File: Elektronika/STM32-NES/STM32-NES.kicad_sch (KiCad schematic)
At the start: 8 parts, among them J1 LCD Display 2.8 Cala, J2 Power Supply 5V 3A, J3 PAD, U1 NUCLEO-F446RE

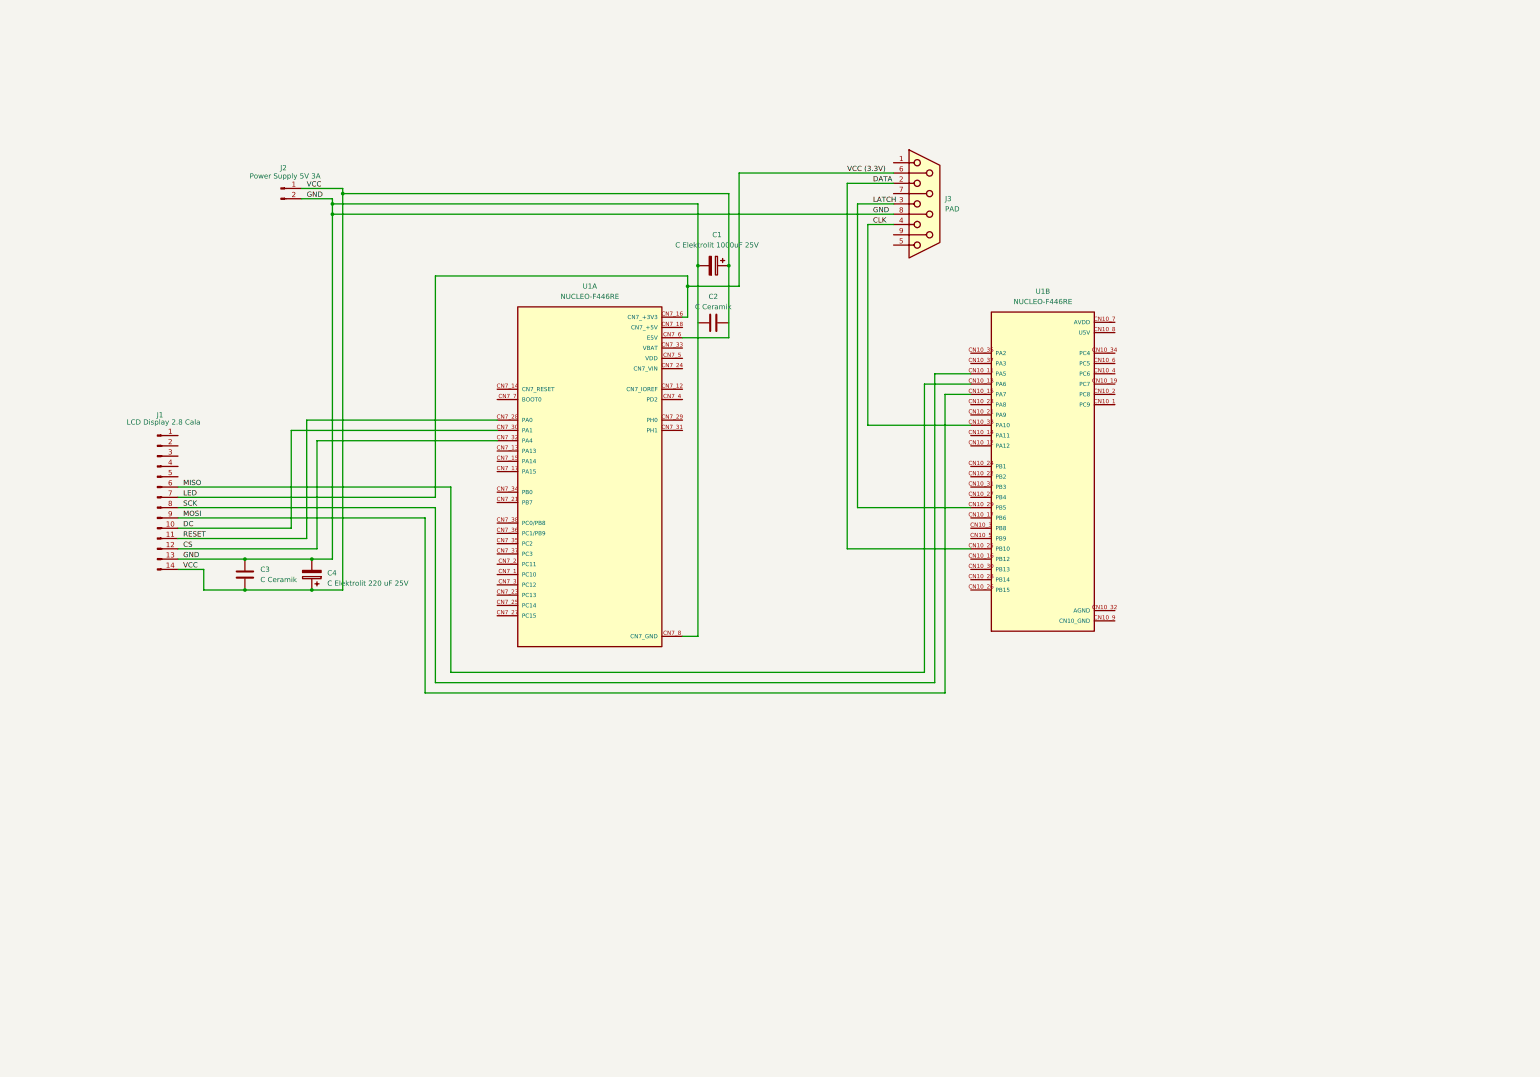
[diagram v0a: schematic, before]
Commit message: I2S przeniesiono z I2S2 na I2S3 eliminując szumy z SPI1. Bufor sampli muzyki w SRAM2, dzięki czemu DMA do LCD i DMA po I2S może chodzić równolegle.
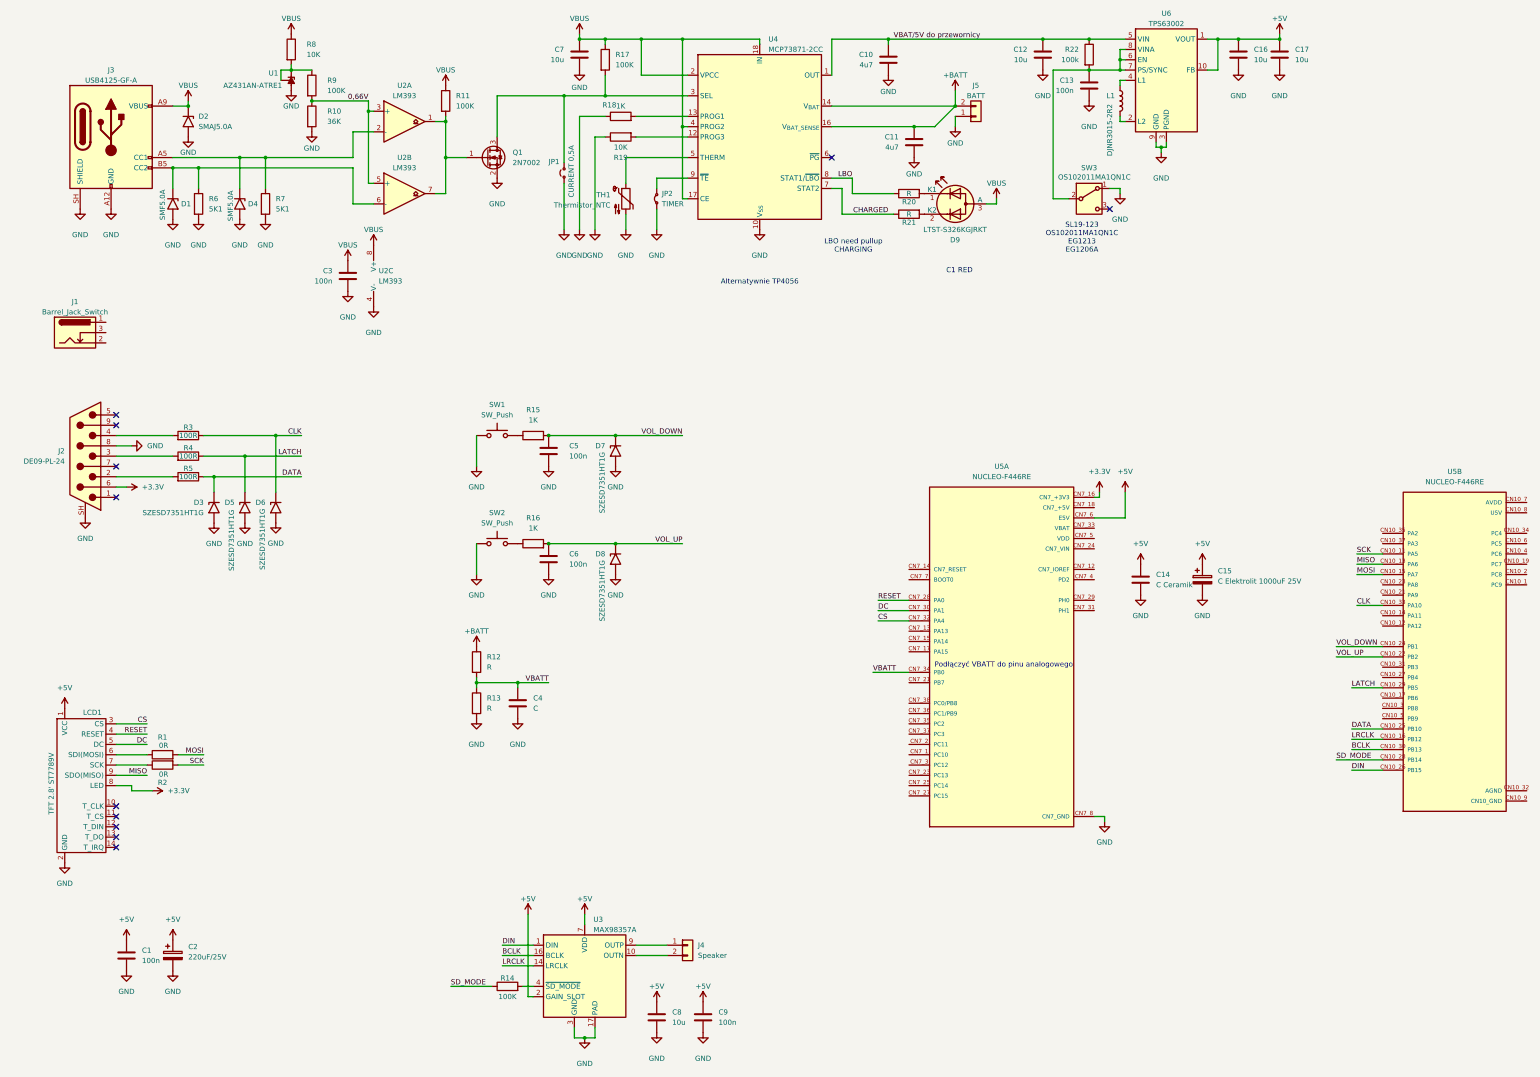
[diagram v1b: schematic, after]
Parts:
- removed C1: C Elektrolit 1000uF 25V, symbol Device:C_Polarized
- removed C4: C Elektrolit 220 uF 25V, symbol Device:C_Polarized
- removed J1: LCD Display 2.8 Cala, symbol Connector:Conn_01x14_Pin
- removed J2: Power Supply 5V 3A, symbol Connector:Conn_01x02_Pin
- removed J3: PAD, symbol Connector:DE9_Socket
- added C1, C13, C5, C6: 100n, symbol Device:C
- added C10: 4u7, Capacitor_SMD:C_0805_2012Metric, symbol Device:C
- added C11: 4u7, symbol Device:C
- added C12: 10u, symbol Device:C
- added C15: C Elektrolit 1000uF 25V, symbol Device:C_Polarized
- added C16, C17, C7, C8: 10u, Capacitor_SMD:C_0805_2012Metric, symbol Device:C
- added C2: 220uF/25V, symbol Device:C_Polarized
- added C4: C, symbol Device:C
- added C9: 100n, Capacitor_SMD:C_0805_2012Metric, symbol Device:C
- added D1, D4: SMF5.0A, Diode_SMD:D_SOD-123F, symbol Diode:SMF5V0A
- added D2: SMAJ5.0A, Diode_SMD:D_SMA, symbol Diode:SMAJ5.0A
- added D3, D5, D6, D7, D8: SZESD7351HT1G, Diode_SMD:D_SOD-323_HandSoldering, symbol Diode:SMF5V0A
- added D9: LTST-S326KGJRKT, LED_SMD:LED_LiteOn_LTST-S326, symbol Device:LED_Dual_KKA
- added J1: Barrel_Jack_Switch, symbol Connector:Barrel_Jack_Switch
- added J2: DE09-PL-24, Connector_Dsub:DSUB-9_Pins_Horizontal_P2.77x2.84mm_EdgePinOffset4.94mm_Housed_MountingHolesOffset4.94mm, symbol Connector:DE9_Pins_MountingHoles
- added J3: USB4125-GF-A, Connector_USB:USB_C_Receptacle_HRO_TYPE-C-31-M-17, symbol Connector:USB_C_Receptacle_PowerOnly_6P
- added J4: Speaker, Connector_JST:JST_PH_B2B-PH-K_1x02_P2.00mm_Vertical, symbol Connector_Generic:Conn_01x02
- added J5: BATT, Connector_JST:JST_PH_B2B-PH-K_1x02_P2.00mm_Vertical, symbol Connector_Generic:Conn_01x02
- added JP1: CURRENT 0,5A, symbol Jumper:Jumper_2_Small_Open
- added JP2: TIMER, symbol Jumper:Jumper_2_Small_Bridged
- added L1: DJNR3015-2R2, Inductor_SMD:L_Coilcraft_LPS3010, symbol Device:L
- added LCD1: TFT 2.8' ST7789V, STM32-NES:TFT 2.8' ST7789V, symbol STM32-NES:TFT_240x320_2.8{dblquote}_SPI_ST7789V
- added Q1: 2N7002, Package_TO_SOT_SMD:SOT-23, symbol Transistor_FET:2N7002
- added R1, R2: 0R, symbol Device:R
- added R10: 36K, symbol Device:R
- added R11, R14, R17, R9: 100K, symbol Device:R
- added R12, R13, R20, R21: R, symbol Device:R
- added R15, R16, R18: 1K, symbol Device:R
- added R19, R8: 10K, symbol Device:R
- added R22: 100k, symbol Device:R
- added R3, R4, R5: 100R, symbol Device:R
- added R6, R7: 5K1, symbol Device:R
- added SW1, SW2: SW_Push, symbol Switch:SW_Push
- added SW3: OS102011MA1QN1C, Button_Switch_THT:SW_Slide_SPDT_Angled_CK_OS102011MA1Q, symbol Switch:SW_SPDT
- added TH1: Thermistor_NTC, symbol Device:Thermistor_NTC
- added U1: AZ431AN-ATRE1, Package_TO_SOT_SMD:SOT-23, symbol Reference_Voltage:TL432DBZ
- added U2: LM393, symbol Comparator:LM393
- added U3: MAX98357A, Package_DFN_QFN:TQFN-16-1EP_3x3mm_P0.5mm_EP1.23x1.23mm, symbol Audio:MAX98357A
- added U4: MCP73871-2CC, Package_DFN_QFN:QFN-20-1EP_4x4mm_P0.5mm_EP2.5x2.5mm, symbol Battery_Management:MCP73871-2CC
- added U6: TPS63002, Package_SON:Texas_DRC0010J_ThermalVias, symbol Regulator_Switching:TPS63002
- C3: value C Ceramik -> 100n
- U5: renamed from U1; footprint NUCLEO-F446RE:MODULE_NUCLEO-F446RE -> NUCLEO F446:MODULE_NUCLEO-F446RE
- renumbered C2 to C14
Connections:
- net CLK: now also D6.1 (A1), R3.1
- net CN7_GND: now also C14.1, C1.1, C10.2, C11.2, C12.2, C13.2, C15.2, C16.2, C17.2, C2.2, C4.2, C5.2, C6.2, C7.2, C8.2, C9.2, D1.2 (A2), D2.2 (A2), D3.2 (A2), D4.2 (A2), D5.2 (A2), D7.2 (A2), D8.2 (A2), J2.8, J2.SH (PAD), J3.A12 (GND), J3.B12 (GND), J3.SH (SHIELD), J5.1 (Pin_1), JP1.1 (A), JP2.1 (A), LCD1.2 (GND), Q1.2 (S), R10.2, R13.2, R18.1, R19.1, R6.2, R7.2, SW1.1, SW2.1, SW3.1 (A), TH1.2, U1.3 (A), U2.4 (V-), U3.11 (GND), U3.15 (GND), U3.17 (PAD), U3.3 (GND), U4.10 (V_{SS}), U4.11 (V_{SS}), U4.21 (V_{SS}), U6.11 (PGND), U6.3 (PGND), U6.9 (GND)
- net CS: now also LCD1.3 (CS)
- net DATA: now also D3.1 (A1), R5.1
- net DC: now also LCD1.5 (DC)
- net LATCH: now also D5.1 (A1), R4.1
- net MISO: now also LCD1.9 (SDO(MISO))
- net MOSI: now also R1.2
- net RESET: now also LCD1.4 (RESET)
- net SCK: now also R2.2
- net LRCLK: now reaches U5.CN10_16 (PB12)
- net LRCLK: now also U3.14 (LRCLK)
- net VOL_UP: now reaches U5.CN10_22 (PB2)
- net VOL_UP: now also C6.1, D8.1 (A1), R16.2
- net VOL_DOWN: now reaches U5.CN10_24 (PB1)
- net VOL_DOWN: now also C5.1, D7.1 (A1), R15.2
- net DIN: now reaches U5.CN10_26 (PB15)
- net DIN: now also U3.1 (DIN)
- net SD_MODE: now reaches U5.CN10_28 (PB14)
- net SD_MODE: now also R14.1
- net BCLK: now reaches U5.CN10_30 (PB13)
- net BCLK: now also U3.16 (BCLK)
- net VBATT: now reaches U5.CN7_34 (PB0)
- net VBATT: now also C4.1, R12.2, R13.1
- net +5V: now reaches C14.2
- net +5V: now also U5.CN7_6 (E5V), C1.2, C15.1, C16.1, C17.1, C2.1, C8.1, C9.1, LCD1.1 (VCC), U3.2 (GAIN_SLOT), U3.7 (VDD), U3.8 (VDD), U6.1 (VOUT), U6.10 (FB)
- net LED renamed +3.3V
- net +3.3V: now also J2.6, LCD1.8 (LED)
- net VCC renamed VBUS
- net VBUS: now also C7.1, D2.1 (A1), D9.3 (A), J3.A9 (VBUS), J3.B9 (VBUS), R11.1, R17.1, R8.1, U2.8 (V+), U4.17 (CE), U4.18 (IN), U4.19 (IN), U4.2 (VPCC), U4.4 (PROG2); no longer U5.CN7_6 (E5V)
- new net: J2.4, R3.2
- new net: LCD1.6 (SDI(MOSI)), R1.1
- new net: R15.1, SW1.2
- new net: R19.2, U4.12 (PROG3)
- new net: R18.2, U4.13 (PROG1)
- new net: JP1.2 (B), Q1.3 (D), R17.2, U4.3 (SEL)
- new net: TH1.1, U4.5 (THERM)
- new net: JP2.2 (B), U4.9 (~{TE})
- new net: J2.2, R5.2
- new net: C13.1, R22.2, SW3.2 (B), U6.6 (EN), U6.7 (PS/SYNC), U6.8 (VINA)
- new net: J2.3, R4.2
- new net: Q1.1 (G), R11.2, U2.1, U2.7
- new net: D4.1 (A1), J3.A5 (CC1), R7.1, U2.2 (-)
- new net: J4.2 (Pin_2), U3.10 (OUTN)
- new net: R14.2, U3.4 (~{SD_MODE})
- new net: J4.1 (Pin_1), U3.9 (OUTP)
- new net: D1.1 (A1), J3.B5 (CC2), R6.1, U2.6 (-)
- new net: D9.1 (K1), R20.2
- new net: D9.2 (K2), R21.2
- new net: R8.2, R9.1, U1.1 (REF), U1.2 (K)
- new net: L1.1, U6.4 (L1)
- new net: L1.2, U6.2 (L2)
- new net: R16.1, SW2.2
- new net: LCD1.7 (SCK), R2.1
- new net +BATT: C11.1, J5.2 (Pin_2), R12.1, U4.14 (V_{BAT}), U4.15 (V_{BAT}), U4.16 (V_{BAT_SENSE})
- new net 0,66V: R10.1, R9.2, U2.3 (+), U2.5 (+)
- new net CHARGED: R21.1, U4.7 (STAT2)
- new net LBO: R20.1, U4.8 (STAT1/~{LBO})
- new net VBAT/5V do przewornicy: C10.1, C12.1, R22.1, U4.1 (OUT), U4.20 (OUT), U6.5 (VIN)
- no-connect marks 0 -> 11
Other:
- note added: "Alternatywnie TP4056"
- note added: "C1 RED"
- note added: "LBO need pullup CHARGING"
- note added: "Podłączyć VBATT do pinu analogowego"
- note added: "SL19-123 OS102011MA1QN1C EG1213 EG1206A"
- company: (none) -> Tomasz Łukomski
- title: (none) -> STM32-NES
- moved on the sheet: C14, U5A, U5B
